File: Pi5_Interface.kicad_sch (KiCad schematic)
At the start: 6 parts, among them J13 Pi 5 UART, J14 Pi 5 power

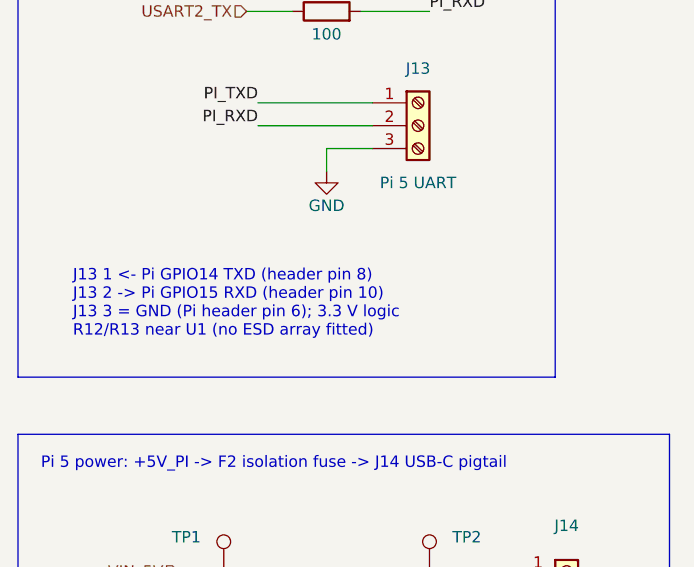
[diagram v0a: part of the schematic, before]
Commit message: Place LED and resistor groups, route 3.3 V rails, relabel LEDs
Layout:
- Place D5, TP3, UART series resistors R12/R13 and resistors R3,
  R17-R22, R24 and R26-R33.
- Move C1, and the motor-side regulators U6/U7 with C34/C35.
- Route +3V3, +3.3VA, BOOT and GND tracks; add one copper zone.
- Rename the power/status LED references to rail names
  (D3 -> 3V3, D4 -> 12V, D6 -> AUX, D7 -> SYS, D8 -> HB, D9 -> PI,
  D11 -> MOT). These no longer match the schematic references.
- Unlock the previously locked placements for rework.

Schematic:
- Shorten the J13 note in Pi5_Interface (drop the Pi header pin
  numbers for TXD/RXD).

Co-Authored-By: Claude Opus 5.5 <noreply@anthropic.com>
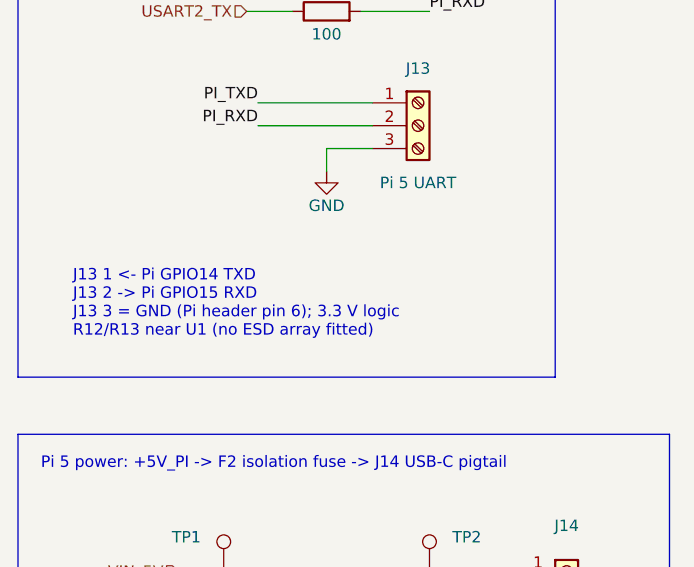
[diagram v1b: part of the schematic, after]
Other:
- note added: "J13 1 <- Pi GPIO14 TXD J13 2 -> Pi GPIO15 RXD J13 3 = GND (Pi header pin 6); 3.3 V logic R12/R13 near U1 (no ESD array fitted)"
- note removed: "J13 1 <- Pi GPIO14 TXD (header pin 8) J13 2 -> Pi GPIO15 RXD (header pin 10) J13 3 = GND (Pi header pin 6); 3.3 V logic R12/R13 near U1 (no ESD array fitted)"
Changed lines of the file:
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@@
 		)
 	)
-	(text "J13 1 <- Pi GPIO14 TXD (header pin 8)\nJ13 2 -> Pi GPIO15 RXD (header pin 10)\nJ13 3 = GND (Pi header pin 6); 3.3 V logic\nR12/R13 near U1 (no ESD array fitted)"
+	(text "J13 1 <- Pi GPIO14 TXD\nJ13 2 -> Pi GPIO15 RXD\nJ13 3 = GND (Pi header pin 6); 3.3 V logic\nR12/R13 near U1 (no ESD array fitted)"
 		(exclude_from_sim no)
 		(at 53.09 90.93 0)

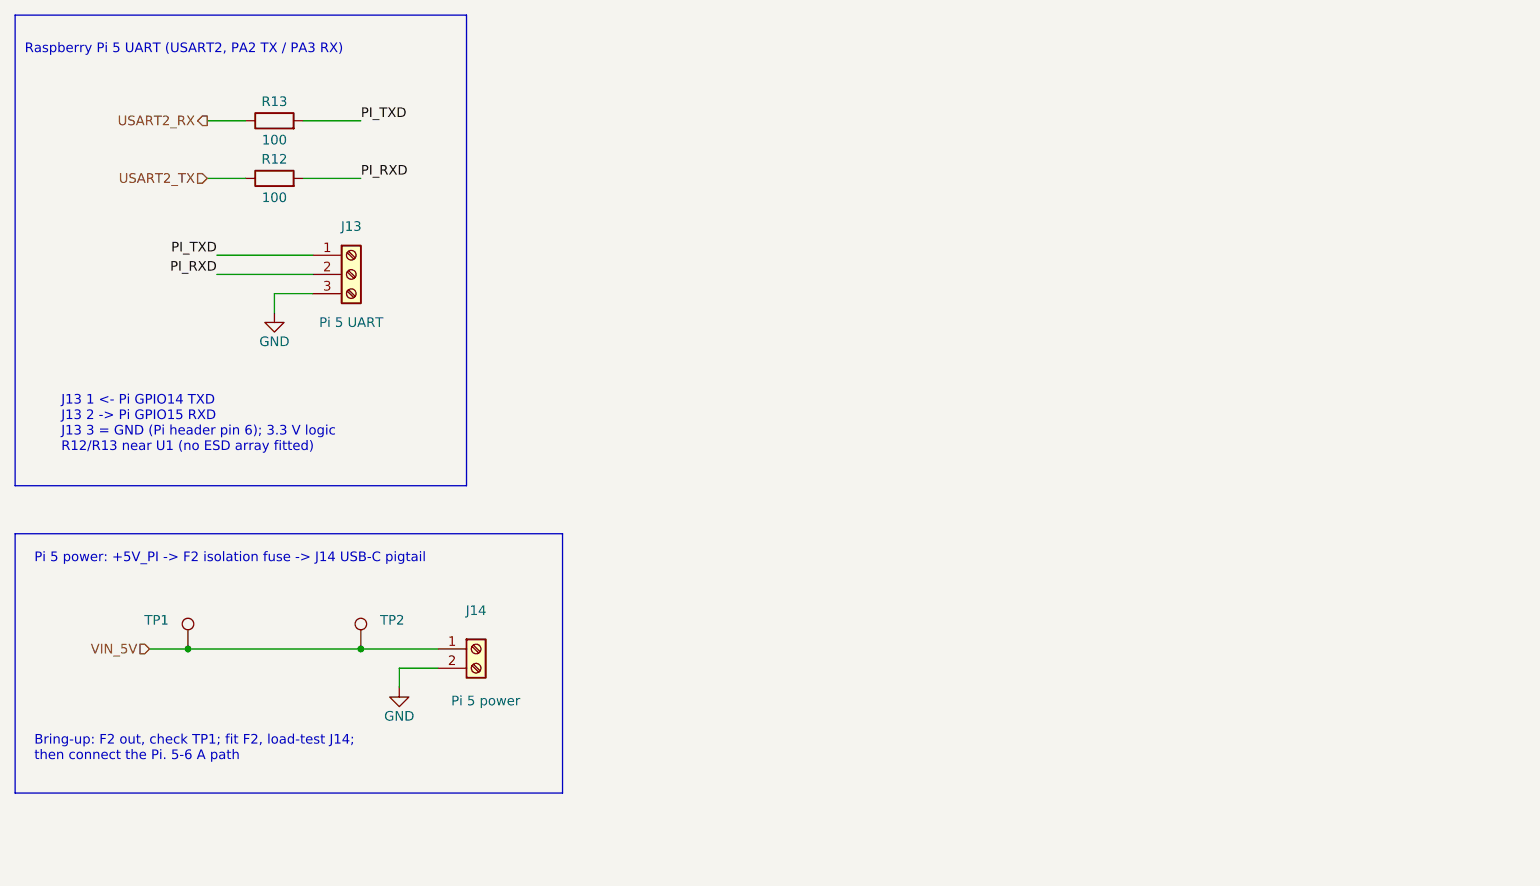
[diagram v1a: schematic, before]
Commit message: Add input protection, AUX ports, servo interface and Pi control
Implements the 2026-10-15 design review decisions in the schematic.
ERC 0 errors, 0 warnings.

New sheets:
- Input Protection: Q1 SQJ409EP reverse-battery P-FET after F1 (D12
  12 V gate clamp, R36), D13 SMBJ16A TVS on +12V, battery sense
  R37/R38/C37 -> VBAT_SENSE on PA0. PWR_FLAG moves to +12V.
- AUX Outputs: four +5V_AUX ports J18-J21 (JST XH 2-pin: Notecard,
  LiDAR, GNSS, IMU), each through a 1.5 A PTC (F4-F7).
- Servo Interface: J17 (GND, VBAT_SERVO via F3 5 A fuse, SERVO_SIG) for
  the Hiwonder HTS-30HS through an external 11.1-12 V buck. U8
  SN74LVC1T45 translates PB10 (USART3 half-duplex) to the 5 V bus,
  PB11 sets direction; R39-R42 pull-ups/series, D14 ESD.

Root sheet:
- F1 output is now VBAT_FUSED; C36 sits on +12V after Q1. J2-F1 net
  named VBAT_IN. F1 7.5 A -> 10 A (0297010.L).
- Y3/C5/C6 fitted (were DNP).
- PA0 -> VBAT_SENSE, PA1 -> PI_3V3_SENSE, PB10 -> SERVO_TX,
  PB11 -> SERVO_DIR. Notes updated (no more F2 / XT30-only text).

Pi 5 Interface:
- J13 -> 6-pin JST XH: TXD, RXD, GND, PI_3V3, PI_RESET, PI_BOOT0.
- PI_3V3 -> D15 -> AUX_EN (U5 enable) and R44/R45 -> PA1.
- PI_RESET -> Q2 DMN63D8L -> NRST (open drain, R46 pull-down).
- PI_BOOT0 -> R47 1k -> BOOT0, for reflashing over USART2.
- R12/R13 100R -> 1k (PA2/PA3 are TTa, 5 mA injection max).
- Remove TP2 (same net as TP1 since F2 was removed).

Buck 5V AUX: U5 EN from AUX_EN (was +12V), R43 100k pull-down, C40,
J22 force-on jumper. Buck 5V SYS: C49 100 nF at U3 VIN/GND.
U2/U5 value TPSM63606RDLR; VCC design note corrected (internal 1 uF,
must stay NC).

Motor Control (now A3):
- U9/U10 74LVC2G17 encoder buffers on +3V3; encoder series R 100R ->
  1k with C43-C46 1 nF; R48-R51 4.7k pull-ups (DNP).
- F8/F9 0.2 A PTC + C47/C48 on each encoder supply (ENC1_5V, ENC2_5V).
- J7/J15 pin order 5V, GND, A, B (matches the am-3651 plug).
- R52/R53 10k pull-downs on both PWM lines (MDD20A brakes on low).
- F10/F11 PTC in series with J6/J16 p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
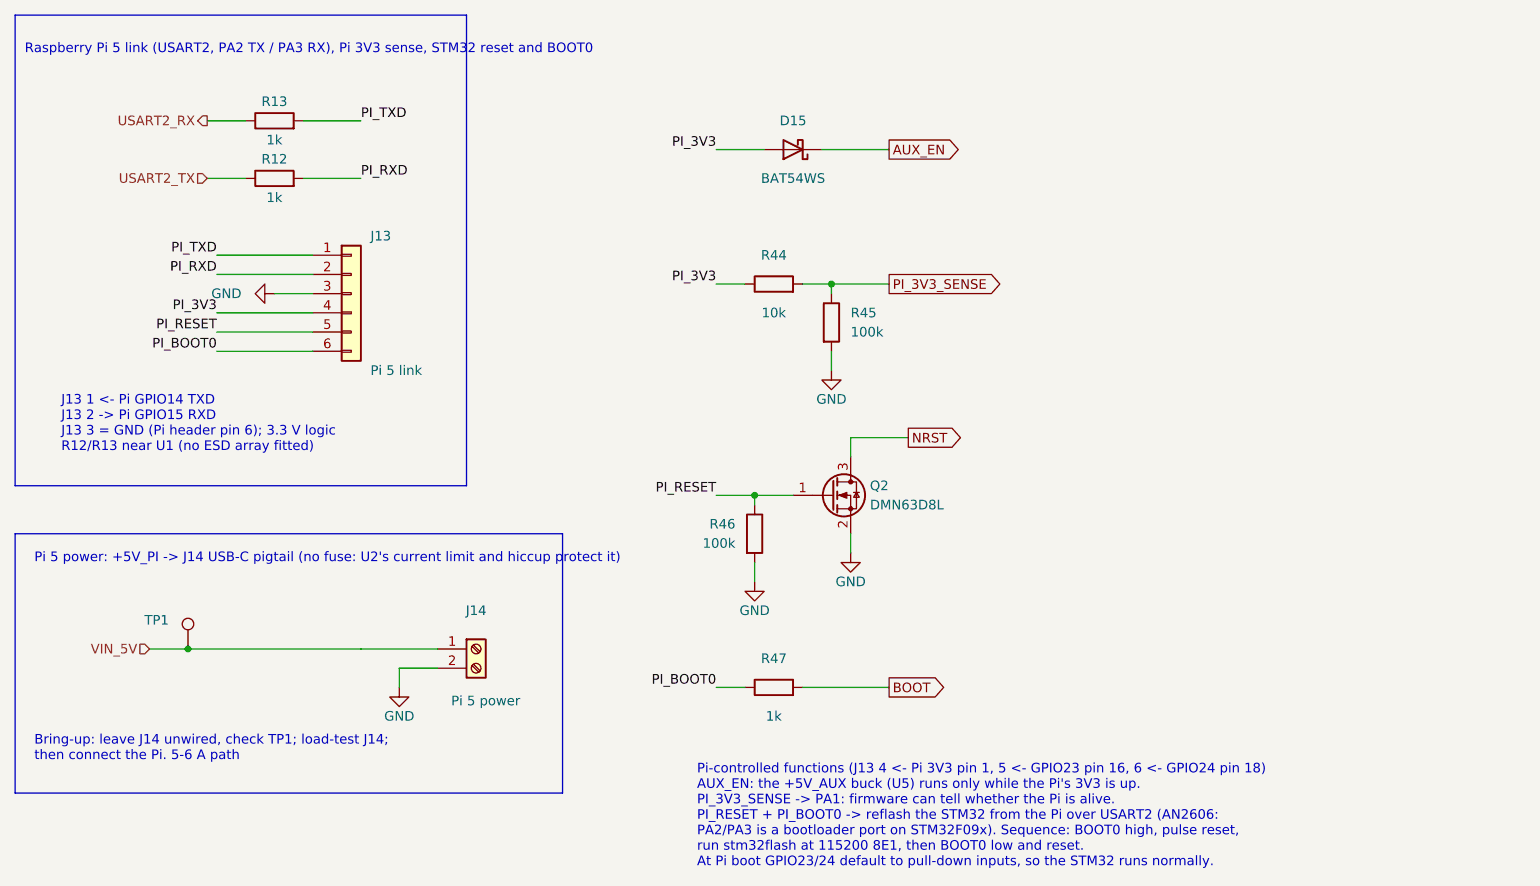
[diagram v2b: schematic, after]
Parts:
- removed TP2: PI_5V, TestPoint:TestPoint_Keystone_5000-5004_Miniature, symbol Connector:TestPoint
- added D15: BAT54WS, Diode_SMD:D_SOD-323, symbol Device:D_Schottky
- added Q2: DMN63D8L, Package_TO_SOT_SMD:SOT-23, symbol Transistor_FET:2N7002
- added R44: 10k, Resistor_SMD:R_0805_2012Metric, symbol Device:R
- added R45, R46: 100k, Resistor_SMD:R_0805_2012Metric, symbol Device:R
- added R47: 1k, Resistor_SMD:R_0805_2012Metric, symbol Device:R
- J13: value Pi 5 UART -> Pi 5 link; footprint TerminalBlock_Phoenix:TerminalBlock_Phoenix_MKDS-1,5-3_1x03_P5.00mm_Horizontal -> Connector_JST:JST_XH_S6B-XH-A_1x06_P2.50mm_Horizontal; symbol Connector:Screw_Terminal_01x03 -> Connector_Generic:Conn_01x06; MPN 1715035 (MKDS 1,5/3, 5.0 mm pitch) -> S6B-XH-A(LF)(SN); Manufacturer Phoenix Contact -> JST; Mating (none) -> XHP-6 housing + 6x SXH-001T-P0.6 crimp (AWG 28-22); Rating 17.5 A / 250 V (IEC), 26-14 AWG; used for 3.3 V UART signals -> (none)
- R12, R13: value 100 -> 1k
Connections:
- net GND: now also Q2.2 (S), R45.2, R46.2
- new net AUX_EN: D15.1 (K)
- new net BOOT: R47.2
- new net NRST: Q2.3 (D)
- new net PI_3V3: D15.2 (A), J13.4 (Pin_4), R44.1
- new net PI_3V3_SENSE: R44.2, R45.1
- new net PI_BOOT0: J13.6 (Pin_6), R47.1
- new net PI_RESET: J13.5 (Pin_5), Q2.1 (G), R46.1
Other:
- note added: "Bring-up: leave J14 unwired, check TP1; load-test J14; then connect the Pi. 5-6 A path"
- note added: "Pi 5 power: +5V_PI -> J14 USB-C pigtail (no fuse: U2's current limit and hiccup protect it)"
- note added: "Pi-controlled functions (J13 4 <- Pi 3V3 pin 1, 5 <- GPIO23 pin 16, 6 <- GPIO24 pin 18) AUX_EN: the +5V_AUX buck (U5) runs only while the Pi's 3V3 is up. PI_3V3_SENSE -> PA1: firmware can tell whether the Pi is alive. PI_RESET + PI_BOOT0 -> reflash the STM32 from the Pi over USART2 (AN2606: PA2/PA3 is a bootloader port on STM32F09x). Sequence: BOOT0 high, pulse reset, run stm32flash at 115200 8E1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"
- note added: "Raspberry Pi 5 link (USART2, PA2 TX / PA3 RX), Pi 3V3 sense, STM32 reset and BOOT0"
- note removed: "Bring-up: F2 out, check TP1; fit F2, load-test J14; then connect the Pi. 5-6 A path"
- note removed: "Pi 5 power: +5V_PI -> F2 isolation fuse -> J14 USB-C pigtail"
- note removed: "Raspberry Pi 5 UART (USART2, PA2 TX / PA3 RX)"
